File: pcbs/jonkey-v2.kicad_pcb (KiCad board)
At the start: 2 copper layers, 191.4 x 129.7 mm, 155 parts

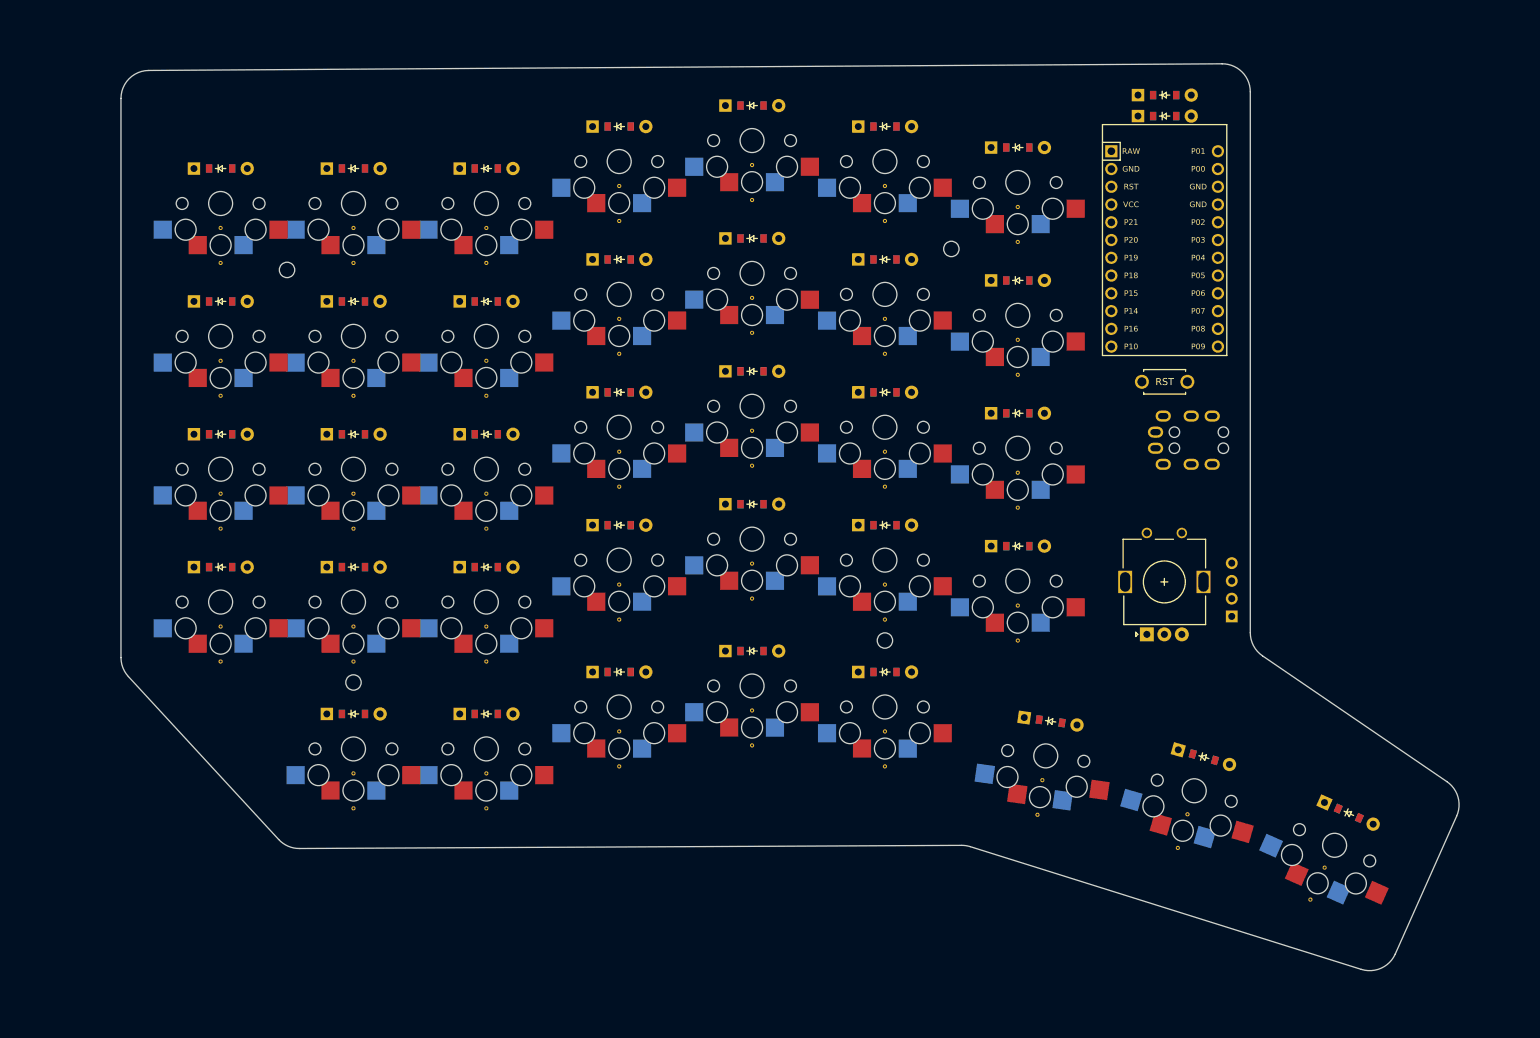
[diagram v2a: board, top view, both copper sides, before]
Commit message: feat: shift thumb column pins to free up 1 pin
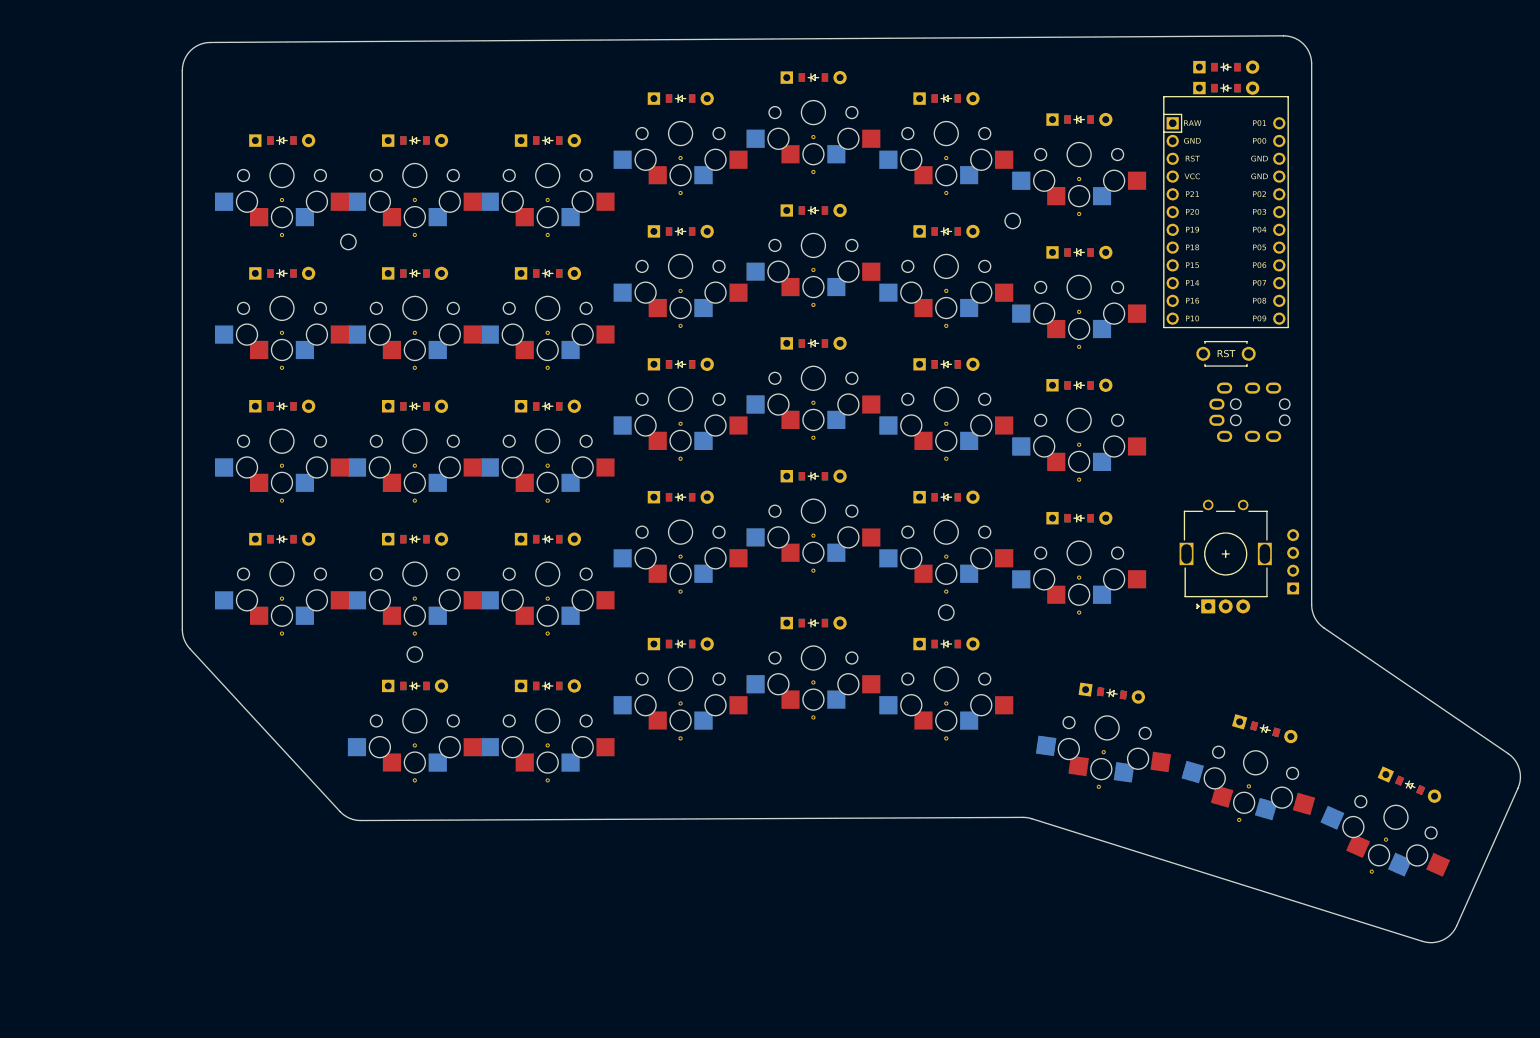
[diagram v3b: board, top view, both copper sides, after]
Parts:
- removed the REF** at (239.5, 191.0)
- removed the REF** at (179.7, 139.1)
- removed the REF** at (259.6, 195.7)
- removed the REF** at (236.7, 147.1)
- removed the REF** at (179.7, 184.1)
- removed the REF** at (280.6, 198.5)
- removed the REF** at (236.7, 109.0)
- removed the REF** at (160.7, 131.1)
- removed the REF** at (141.7, 107.0)
- removed the REF** at (160.7, 169.1)
- removed the REF** at (160.7, 126.0)
- removed the REF** at (179.7, 101.0)
- removed the REF** at (122.7, 164.1)
- removed the REF** at (198.7, 181.1)
- removed the REF** at (217.7, 139.1)
- removed the REF** at (179.7, 144.1)
- removed the REF** at (122.7, 145.1)
- removed the REF** at (179.7, 163.1)
- removed the REF** at (217.7, 101.0)
- removed the REF** at (198.7, 155.1)
- removed the REF** at (198.7, 176.1)
- removed the REF** at (217.7, 120.0)
- removed the REF** at (122.7, 107.0)
- removed the REF** at (217.7, 125.0)
- removed the REF** at (261.0, 190.9)
- removed the REF** at (141.7, 164.1)
- removed the REF** at (240.2, 186.0)
- removed the REF** at (198.7, 117.0)
- removed the REF** at (179.7, 158.1)
- removed the REF** at (198.7, 98.0)
- removed the REF** at (160.7, 145.1)
- removed the REF** at (141.7, 150.1)
- removed the REF** at (198.7, 136.1)
- removed the REF** at (236.7, 104.0)
- removed the REF** at (217.7, 144.1)
- removed the REF** at (141.7, 131.1)
- removed the REF** at (179.7, 179.1)
- removed the REF** at (179.7, 120.0)
- removed the REF** at (141.7, 185.1)
- removed the REF** at (278.6, 203.1)
- removed the REF** at (122.7, 150.1)
- removed the REF** at (217.7, 163.1)
- removed the REF** at (198.7, 160.1)
- removed the REF** at (141.7, 190.1)
- removed the REF** at (198.7, 141.1)
- removed the REF** at (122.7, 169.1)
- removed the REF** at (122.7, 131.1)
- removed the REF** at (122.7, 112.0)
- removed the REF** at (236.7, 161.1)
- removed the REF** at (141.7, 169.1)
- removed the REF** at (179.7, 106.0)
- removed the REF** at (217.7, 179.1)
- removed the REF** at (160.7, 107.0)
- removed the REF** at (236.7, 128.1)
- removed the REF** at (217.7, 106.0)
- removed the REF** at (217.7, 184.1)
- removed the REF** at (179.7, 125.0)
- removed the REF** at (141.7, 145.1)
- removed the REF** at (236.7, 166.1)
- removed the REF** at (198.7, 122.0)
- removed the REF** at (141.7, 126.0)
- removed the REF** at (236.7, 142.1)
- removed the REF** at (122.7, 126.0)
- removed the REF** at (160.7, 164.1)
- removed the REF** at (160.7, 112.0)
- removed the REF** at (198.7, 103.0)
- removed the REF** at (236.7, 123.0)
- removed the REF** at (141.7, 112.0)
- removed the REF** at (160.7, 150.1)
- removed the REF** at (217.7, 158.1)
- removed the REF** at (160.7, 190.1)
- removed the REF** at (160.7, 185.1)
- added REF**: VIA-0.6mm, VIA-0.6mm, F.Cu at (245.5, 162.1)
- added REF**: VIA-0.6mm, VIA-0.6mm, F.Cu at (245.5, 100.0)
- added REF**: VIA-0.6mm, VIA-0.6mm, F.Cu at (268.4, 191.7)
- added REF**: VIA-0.6mm, VIA-0.6mm, F.Cu at (150.5, 160.1)
- added REF**: VIA-0.6mm, VIA-0.6mm, F.Cu at (207.5, 177.1)
- added REF**: VIA-0.6mm, VIA-0.6mm, F.Cu at (207.5, 113.0)
- added REF**: VIA-0.6mm, VIA-0.6mm, F.Cu at (226.5, 140.1)
- added REF**: VIA-0.6mm, VIA-0.6mm, F.Cu at (207.5, 118.0)
- added REF**: VIA-0.6mm, VIA-0.6mm, F.Cu at (131.5, 108.0)
- added REF**: VIA-0.6mm, VIA-0.6mm, F.Cu at (169.5, 122.0)
- added REF**: VIA-0.6mm, VIA-0.6mm, F.Cu at (245.5, 105.0)
- added REF**: VIA-0.6mm, VIA-0.6mm, F.Cu at (169.5, 141.1)
- added REF**: VIA-0.6mm, VIA-0.6mm, F.Cu at (131.5, 141.1)
- added REF**: VIA-0.6mm, VIA-0.6mm, F.Cu at (150.5, 108.0)
- added REF**: VIA-0.6mm, VIA-0.6mm, F.Cu at (289.4, 194.5)
- added REF**: VIA-0.6mm, VIA-0.6mm, F.Cu at (150.5, 141.1)
- added REF**: VIA-0.6mm, VIA-0.6mm, F.Cu at (226.5, 102.0)
- added REF**: VIA-0.6mm, VIA-0.6mm, F.Cu at (131.5, 103.0)
- added REF**: VIA-0.6mm, VIA-0.6mm, F.Cu at (188.5, 97.0)
- added REF**: VIA-0.6mm, VIA-0.6mm, F.Cu at (188.5, 102.0)
- added REF**: VIA-0.6mm, VIA-0.6mm, F.Cu at (188.5, 154.1)
- added REF**: VIA-0.6mm, VIA-0.6mm, F.Cu at (150.5, 165.1)
- added REF**: VIA-0.6mm, VIA-0.6mm, F.Cu at (287.3, 199.1)
- added REF**: VIA-0.6mm, VIA-0.6mm, F.Cu at (188.5, 140.1)
- added REF**: VIA-0.6mm, VIA-0.6mm, F.Cu at (188.5, 121.0)
- added REF**: VIA-0.6mm, VIA-0.6mm, F.Cu at (169.5, 181.1)
- added REF**: VIA-0.6mm, VIA-0.6mm, F.Cu at (169.5, 186.1)
- added REF**: VIA-0.6mm, VIA-0.6mm, F.Cu at (169.5, 160.1)
- added REF**: VIA-0.6mm, VIA-0.6mm, F.Cu at (245.5, 157.1)
- added REF**: VIA-0.6mm, VIA-0.6mm, F.Cu at (226.5, 116.0)
- added REF**: VIA-0.6mm, VIA-0.6mm, F.Cu at (131.5, 165.1)
- added REF**: VIA-0.6mm, VIA-0.6mm, F.Cu at (169.5, 103.0)
- added REF**: VIA-0.6mm, VIA-0.6mm, F.Cu at (226.5, 180.1)
- added REF**: VIA-0.6mm, VIA-0.6mm, F.Cu at (150.5, 127.0)
- added REF**: VIA-0.6mm, VIA-0.6mm, F.Cu at (269.8, 186.9)
- added REF**: VIA-0.6mm, VIA-0.6mm, F.Cu at (150.5, 186.1)
- added REF**: VIA-0.6mm, VIA-0.6mm, F.Cu at (150.5, 181.1)
- added REF**: VIA-0.6mm, VIA-0.6mm, F.Cu at (207.5, 137.1)
- added REF**: VIA-0.6mm, VIA-0.6mm, F.Cu at (245.5, 124.0)
- added REF**: VIA-0.6mm, VIA-0.6mm, F.Cu at (226.5, 175.1)
- added REF**: VIA-0.6mm, VIA-0.6mm, F.Cu at (169.5, 146.1)
- added REF**: VIA-0.6mm, VIA-0.6mm, F.Cu at (188.5, 180.1)
- added REF**: VIA-0.6mm, VIA-0.6mm, F.Cu at (188.5, 135.1)
- added REF**: VIA-0.6mm, VIA-0.6mm, F.Cu at (226.5, 159.1)
- added REF**: VIA-0.6mm, VIA-0.6mm, F.Cu at (131.5, 160.1)
- added REF**: VIA-0.6mm, VIA-0.6mm, F.Cu at (207.5, 132.1)
- added REF**: VIA-0.6mm, VIA-0.6mm, F.Cu at (207.5, 151.1)
- added REF**: VIA-0.6mm, VIA-0.6mm, F.Cu at (207.5, 172.1)
- added REF**: VIA-0.6mm, VIA-0.6mm, F.Cu at (131.5, 146.1)
- added REF**: VIA-0.6mm, VIA-0.6mm, F.Cu at (245.5, 138.1)
- added REF**: VIA-0.6mm, VIA-0.6mm, F.Cu at (169.5, 127.0)
- added REF**: VIA-0.6mm, VIA-0.6mm, F.Cu at (131.5, 127.0)
- added REF**: VIA-0.6mm, VIA-0.6mm, F.Cu at (188.5, 159.1)
- added REF**: VIA-0.6mm, VIA-0.6mm, F.Cu at (226.5, 121.0)
- added REF**: VIA-0.6mm, VIA-0.6mm, F.Cu at (188.5, 116.0)
- added REF**: VIA-0.6mm, VIA-0.6mm, F.Cu at (207.5, 94.0)
- added REF**: VIA-0.6mm, VIA-0.6mm, F.Cu at (226.5, 97.0)
- added REF**: VIA-0.6mm, VIA-0.6mm, F.Cu at (169.5, 108.0)
- added REF**: VIA-0.6mm, VIA-0.6mm, F.Cu at (169.5, 165.1)
- added REF**: VIA-0.6mm, VIA-0.6mm, F.Cu at (245.5, 143.1)
- added REF**: VIA-0.6mm, VIA-0.6mm, F.Cu at (248.3, 187.0)
- added REF**: VIA-0.6mm, VIA-0.6mm, F.Cu at (226.5, 154.1)
- added REF**: VIA-0.6mm, VIA-0.6mm, F.Cu at (150.5, 103.0)
- added REF**: VIA-0.6mm, VIA-0.6mm, F.Cu at (188.5, 175.1)
- added REF**: VIA-0.6mm, VIA-0.6mm, F.Cu at (150.5, 122.0)
- added REF**: VIA-0.6mm, VIA-0.6mm, F.Cu at (150.5, 146.1)
- added REF**: VIA-0.6mm, VIA-0.6mm, F.Cu at (207.5, 99.0)
- added REF**: VIA-0.6mm, VIA-0.6mm, F.Cu at (226.5, 135.1)
- added REF**: VIA-0.6mm, VIA-0.6mm, F.Cu at (245.5, 119.0)
- added REF**: VIA-0.6mm, VIA-0.6mm, F.Cu at (207.5, 156.1)
- added REF**: VIA-0.6mm, VIA-0.6mm, F.Cu at (131.5, 122.0)
- added REF**: VIA-0.6mm, VIA-0.6mm, F.Cu at (249.0, 182.0)
- moved D35 9.64 mm to (272.1, 178.7)
- moved D36 9.64 mm to (292.8, 186.8)
- moved S36 9.64 mm to (290.8, 191.3)
- moved D17 9.64 mm to (188.5, 126.5)
- moved D27 9.64 mm to (226.5, 126.5)
- moved D1 9.64 mm to (131.5, 151.6)
- moved D10 9.64 mm to (169.5, 172.6)
- moved D11 9.64 mm to (169.5, 151.6)
- moved D12 9.64 mm to (169.5, 132.6)
- moved D13 9.64 mm to (169.5, 113.5)
- moved D14 9.64 mm to (169.5, 94.5)
- moved D15 9.64 mm to (188.5, 166.6)
- moved D16 9.64 mm to (188.5, 145.6)
- moved D18 9.64 mm to (188.5, 107.5)
- moved D19 9.64 mm to (188.5, 88.5)
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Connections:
- S10 pad 2: P15 -> P14
- S15 pad 2: P18 -> P15
- S20 pad 2: P19 -> P18
- S25 pad 2: P20 -> P19
- S34 pad 2: P21 -> P20
- S35 pad 2: P8 -> P21
- S36 pad 2: P9 -> P8
- S5 pad 2: P14 -> P16

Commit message: feat: free up pin 0 incase its needed for serial coms and add access via 4 pins
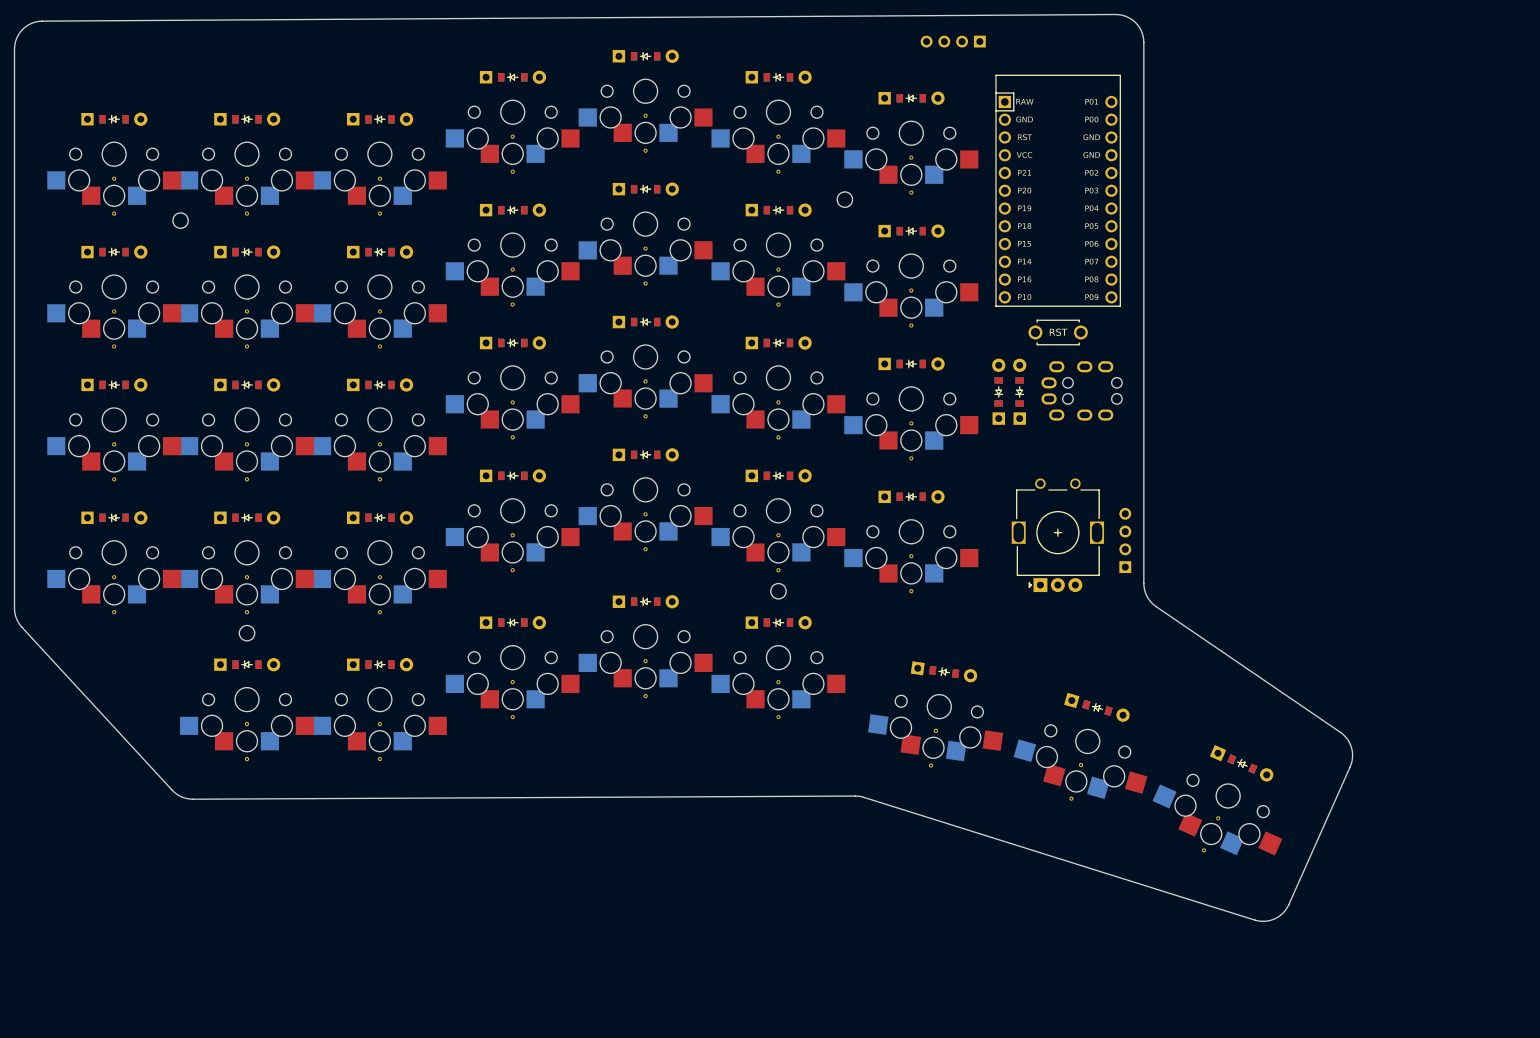
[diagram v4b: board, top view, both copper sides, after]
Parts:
- removed the REF** at (245.5, 162.1)
- removed the REF** at (245.5, 100.0)
- removed the REF** at (268.4, 191.7)
- removed the REF** at (150.5, 160.1)
- removed the REF** at (207.5, 177.1)
- removed the REF** at (207.5, 113.0)
- removed the REF** at (226.5, 140.1)
- removed the REF** at (207.5, 118.0)
- removed the REF** at (131.5, 108.0)
- removed the REF** at (169.5, 122.0)
- removed the REF** at (245.5, 105.0)
- removed the REF** at (169.5, 141.1)
- removed the REF** at (131.5, 141.1)
- removed the REF** at (150.5, 108.0)
- removed the REF** at (289.4, 194.5)
- removed the REF** at (150.5, 141.1)
- removed the REF** at (226.5, 102.0)
- removed the REF** at (131.5, 103.0)
- removed the REF** at (188.5, 97.0)
- removed the REF** at (188.5, 102.0)
- removed the REF** at (188.5, 154.1)
- removed the REF** at (150.5, 165.1)
- removed the REF** at (287.3, 199.1)
- removed the REF** at (188.5, 140.1)
- removed the REF** at (188.5, 121.0)
- removed the REF** at (169.5, 181.1)
- removed the REF** at (169.5, 186.1)
- removed the REF** at (169.5, 160.1)
- removed the REF** at (245.5, 157.1)
- removed the REF** at (226.5, 116.0)
- removed the REF** at (131.5, 165.1)
- removed the REF** at (169.5, 103.0)
- removed the REF** at (226.5, 180.1)
- removed the REF** at (150.5, 127.0)
- removed the REF** at (269.8, 186.9)
- removed the REF** at (150.5, 186.1)
- removed the REF** at (150.5, 181.1)
- removed the REF** at (207.5, 137.1)
- removed the REF** at (245.5, 124.0)
- removed the REF** at (226.5, 175.1)
- removed the REF** at (169.5, 146.1)
- removed the REF** at (188.5, 180.1)
- removed the REF** at (188.5, 135.1)
- removed the REF** at (226.5, 159.1)
- removed the REF** at (131.5, 160.1)
- removed the REF** at (207.5, 132.1)
- removed the REF** at (207.5, 151.1)
- removed the REF** at (207.5, 172.1)
- removed the REF** at (131.5, 146.1)
- removed the REF** at (245.5, 138.1)
- removed the REF** at (169.5, 127.0)
- removed the REF** at (131.5, 127.0)
- removed the REF** at (188.5, 159.1)
- removed the REF** at (226.5, 121.0)
- removed the REF** at (188.5, 116.0)
- removed the REF** at (207.5, 94.0)
- removed the REF** at (226.5, 97.0)
- removed the REF** at (169.5, 108.0)
- removed the REF** at (169.5, 165.1)
- removed the REF** at (245.5, 143.1)
- removed the REF** at (248.3, 187.0)
- removed the REF** at (226.5, 154.1)
- removed the REF** at (150.5, 103.0)
- removed the REF** at (188.5, 175.1)
- removed the REF** at (150.5, 122.0)
- removed the REF** at (150.5, 146.1)
- removed the REF** at (207.5, 99.0)
- removed the REF** at (226.5, 135.1)
- removed the REF** at (245.5, 119.0)
- removed the REF** at (207.5, 156.1)
- removed the REF** at (131.5, 122.0)
- removed the REF** at (249.0, 182.0)
- added REF**: VIA-0.6mm, VIA-0.6mm, F.Cu at (126.5, 178.0)
- added REF**: VIA-0.6mm, VIA-0.6mm, F.Cu at (245.8, 183.8)
- added REF**: VIA-0.6mm, VIA-0.6mm, F.Cu at (107.5, 124.0)
- added REF**: VIA-0.6mm, VIA-0.6mm, F.Cu at (145.5, 138.0)
- added REF**: VIA-0.6mm, VIA-0.6mm, F.Cu at (164.5, 113.0)
- added REF**: VIA-0.6mm, VIA-0.6mm, F.Cu at (224.3, 183.9)
- added REF**: VIA-0.6mm, VIA-0.6mm, F.Cu at (145.5, 105.0)
- added REF**: VIA-0.6mm, VIA-0.6mm, F.Cu at (202.5, 177.0)
- added REF**: VIA-0.6mm, VIA-0.6mm, F.Cu at (202.5, 99.0)
- added REF**: VIA-0.6mm, VIA-0.6mm, F.Cu at (183.5, 174.0)
- added REF**: VIA-0.6mm, VIA-0.6mm, F.Cu at (164.5, 118.0)
- added REF**: VIA-0.6mm, VIA-0.6mm, F.Cu at (183.5, 96.0)
- added REF**: VIA-0.6mm, VIA-0.6mm, F.Cu at (265.4, 191.5)
- added REF**: VIA-0.6mm, VIA-0.6mm, F.Cu at (183.5, 134.0)
- added REF**: VIA-0.6mm, VIA-0.6mm, F.Cu at (221.5, 102.0)
- added REF**: VIA-0.6mm, VIA-0.6mm, F.Cu at (126.5, 105.0)
- added REF**: VIA-0.6mm, VIA-0.6mm, F.Cu at (145.5, 119.0)
- added REF**: VIA-0.6mm, VIA-0.6mm, F.Cu at (164.5, 132.0)
- added REF**: VIA-0.6mm, VIA-0.6mm, F.Cu at (145.5, 162.0)
- added REF**: VIA-0.6mm, VIA-0.6mm, F.Cu at (164.5, 156.0)
- added REF**: VIA-0.6mm, VIA-0.6mm, F.Cu at (126.5, 124.0)
- added REF**: VIA-0.6mm, VIA-0.6mm, F.Cu at (202.5, 137.0)
- added REF**: VIA-0.6mm, VIA-0.6mm, F.Cu at (126.5, 100.0)
- added REF**: VIA-0.6mm, VIA-0.6mm, F.Cu at (202.5, 156.0)
- added REF**: VIA-0.6mm, VIA-0.6mm, F.Cu at (263.3, 196.0)
- added REF**: VIA-0.6mm, VIA-0.6mm, F.Cu at (183.5, 115.0)
- added REF**: VIA-0.6mm, VIA-0.6mm, F.Cu at (221.5, 154.0)
- added REF**: VIA-0.6mm, VIA-0.6mm, F.Cu at (107.5, 162.0)
- added REF**: VIA-0.6mm, VIA-0.6mm, F.Cu at (221.5, 159.0)
- added REF**: VIA-0.6mm, VIA-0.6mm, F.Cu at (107.5, 100.0)
- added REF**: VIA-0.6mm, VIA-0.6mm, F.Cu at (126.5, 183.0)
- added REF**: VIA-0.6mm, VIA-0.6mm, F.Cu at (221.5, 97.0)
- added REF**: VIA-0.6mm, VIA-0.6mm, F.Cu at (221.5, 121.0)
- added REF**: VIA-0.6mm, VIA-0.6mm, F.Cu at (164.5, 172.0)
- added REF**: VIA-0.6mm, VIA-0.6mm, F.Cu at (202.5, 172.0)
- added REF**: VIA-0.6mm, VIA-0.6mm, F.Cu at (126.5, 157.0)
- added REF**: VIA-0.6mm, VIA-0.6mm, F.Cu at (183.5, 110.0)
- added REF**: VIA-0.6mm, VIA-0.6mm, F.Cu at (145.5, 143.0)
- added REF**: VIA-0.6mm, VIA-0.6mm, F.Cu at (202.5, 132.0)
- added REF**: VIA-0.6mm, VIA-0.6mm, F.Cu at (164.5, 177.0)
- added REF**: VIA-0.6mm, VIA-0.6mm, F.Cu at (202.5, 94.0)
- added REF**: VIA-0.6mm, VIA-0.6mm, F.Cu at (107.5, 119.0)
- added REF**: VIA-0.6mm, VIA-0.6mm, F.Cu at (145.5, 100.0)
- added REF**: VIA-0.6mm, VIA-0.6mm, F.Cu at (183.5, 129.0)
- added REF**: VIA-0.6mm, VIA-0.6mm, F.Cu at (107.5, 143.0)
- added REF**: VIA-0.6mm, VIA-0.6mm, F.Cu at (126.5, 119.0)
- added REF**: VIA-0.6mm, VIA-0.6mm, F.Cu at (126.5, 138.0)
- added REF**: VIA-0.6mm, VIA-0.6mm, F.Cu at (202.5, 151.0)
- added REF**: VIA-0.6mm, VIA-0.6mm, F.Cu at (164.5, 137.0)
- added REF**: VIA-0.6mm, VIA-0.6mm, F.Cu at (107.5, 138.0)
- added REF**: VIA-0.6mm, VIA-0.6mm, F.Cu at (221.5, 140.0)
- added REF**: VIA-0.6mm, VIA-0.6mm, F.Cu at (164.5, 99.0)
- added REF**: VIA-0.6mm, VIA-0.6mm, F.Cu at (145.5, 178.0)
- added REF**: VIA-0.6mm, VIA-0.6mm, F.Cu at (145.5, 124.0)
- added REF**: VIA-0.6mm, VIA-0.6mm, F.Cu at (164.5, 151.0)
- added REF**: VIA-0.6mm, VIA-0.6mm, F.Cu at (202.5, 113.0)
- added REF**: VIA-0.6mm, VIA-0.6mm, F.Cu at (164.5, 94.0)
- added REF**: VIA-0.6mm, VIA-0.6mm, F.Cu at (107.5, 105.0)
- added REF**: VIA-0.6mm, VIA-0.6mm, F.Cu at (145.5, 157.0)
- added REF**: VIA-0.6mm, VIA-0.6mm, F.Cu at (183.5, 91.0)
- added REF**: VIA-0.6mm, VIA-0.6mm, F.Cu at (202.5, 118.0)
- added REF**: VIA-0.6mm, VIA-0.6mm, F.Cu at (145.5, 183.0)
- added REF**: VIA-0.6mm, VIA-0.6mm, F.Cu at (183.5, 148.0)
- added REF**: VIA-0.6mm, VIA-0.6mm, F.Cu at (244.4, 188.7)
- added REF**: VIA-0.6mm, VIA-0.6mm, F.Cu at (183.5, 169.0)
- added REF**: VIA-0.6mm, VIA-0.6mm, F.Cu at (107.5, 157.0)
- added REF**: VIA-0.6mm, VIA-0.6mm, F.Cu at (126.5, 162.0)
- added REF**: VIA-0.6mm, VIA-0.6mm, F.Cu at (221.5, 135.0)
- added REF**: VIA-0.6mm, VIA-0.6mm, F.Cu at (183.5, 153.0)
- added REF**: VIA-0.6mm, VIA-0.6mm, F.Cu at (225.0, 179.0)
- added REF**: VIA-0.6mm, VIA-0.6mm, F.Cu at (221.5, 116.0)
- added REF**: VIA-0.6mm, VIA-0.6mm, F.Cu at (126.5, 143.0)
- added SERIAL1: OLED, lib:OLED_headers, F.Cu at (221.5, 82.0)
- moved R11 56.7 mm to (234.0, 130.5), turned to 90 degrees
- moved R21 52.5 mm to (237.0, 130.5), turned to 90 degrees
- moved D35 24.2 mm to (248.1, 175.7)
- moved D1 24.2 mm to (107.5, 148.5)
- moved D10 24.2 mm to (145.5, 169.5)
- moved D11 24.2 mm to (145.5, 148.5)
- moved D12 24.2 mm to (145.5, 129.5)
- moved D13 24.2 mm to (145.5, 110.5)
- moved D14 24.2 mm to (145.5, 91.5)
- moved D15 24.2 mm to (164.5, 163.5)
- moved D16 24.2 mm to (164.5, 142.5)
- moved D17 24.2 mm to (164.5, 123.5)
- moved D18 24.2 mm to (164.5, 104.5)
- moved D19 24.2 mm to (164.5, 85.5)
- moved D2 24.2 mm to (107.5, 129.5)
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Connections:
- ROT1 pad A: P0 -> P9
